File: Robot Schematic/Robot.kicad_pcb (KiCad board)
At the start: 2 copper layers, 64.6 x 60.6 mm, 15 parts, among them J1 Conn_01x04, J2 Conn_01x04, J3 Battery, J4 Switch, J5 Conn_01x06, J6 Conn_01x06, J7 Conn_01x06, U1 mp1584EN

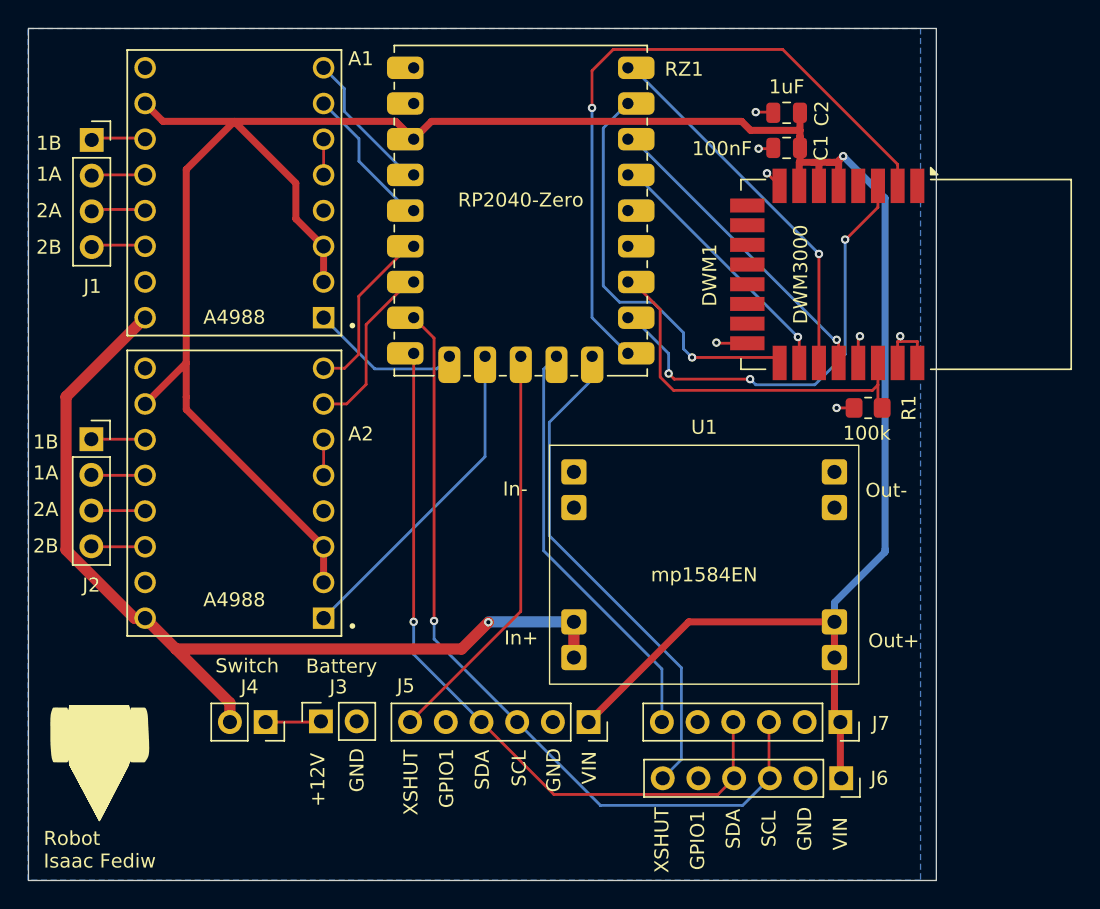
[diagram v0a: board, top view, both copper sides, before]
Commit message: Add DWM Code, Add Transmitter Schematic/PCB
DWM Code features a new library that works and is tested with basic features
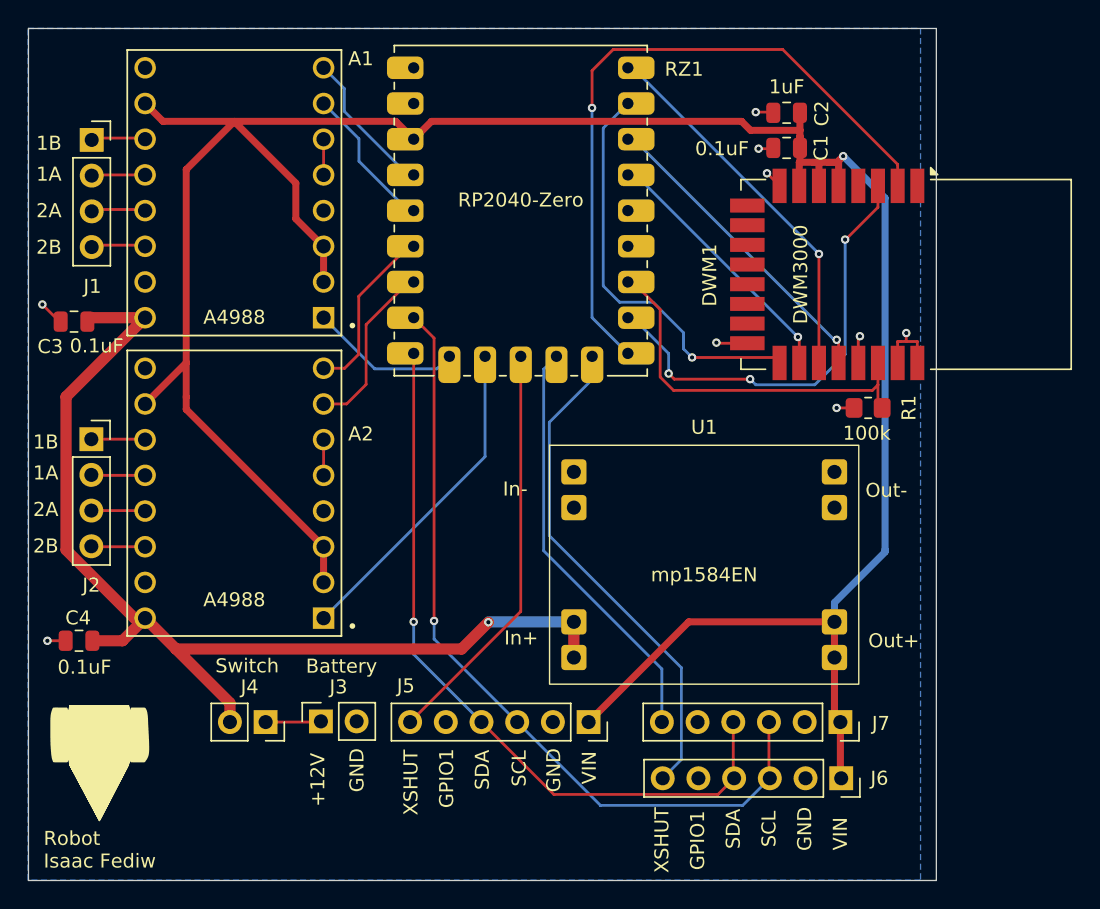
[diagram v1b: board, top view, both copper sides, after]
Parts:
- added C3: 0.1uF, Capacitor_SMD:C_0805_2012Metric, F.Cu at (135.1, 95.7)
- added C4: 0.1uF, Capacitor_SMD:C_0805_2012Metric, F.Cu at (135.4, 118.4)
- C1: value 100nF -> 0.1uF
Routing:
- net +12V: track 68.0 -> 77.3 mm
- net GND: track 13.8 -> 17.2 mm, vias 7 -> 9
